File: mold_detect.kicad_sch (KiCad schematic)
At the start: 22 parts, among them J1 ISP, SW1 watchdog_sw, U1 SHT30-DIS, U2 TPL5010, U3 ATmega328P-P

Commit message: added ces reference; moved sensor to bottom
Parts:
- R1, R2, R3, R4, R5, R6: footprint Resistor_SMD:R_0201_0603Metric -> Resistor_SMD:R_0603_1608Metric
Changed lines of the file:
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@@
       (effects (font (size 1.27 1.27)) (justify left))
     )
-    (property "Footprint" "Resistor_SMD:R_0201_0603Metric" (at 254.762 73.66 90)
+    (property "Footprint" "Resistor_SMD:R_0603_1608Metric" (at 254.762 73.66 90)
       (effects (font (size 1.27 1.27)) hide)
     )
@@
       (effects (font (size 1.27 1.27)) (justify left))
     )
-    (property "Footprint" "Resistor_SMD:R_0201_0603Metric" (at 60.452 170.18 90)
+    (property "Footprint" "Resistor_SMD:R_0603_1608Metric" (at 60.452 170.18 90)
       (effects (font (size 1.27 1.27)) hide)
     )
@@
       (effects (font (size 1.27 1.27)) (justify left))
     )
-    (property "Footprint" "Resistor_SMD:R_0201_0603Metric" (at 93.472 59.69 90)
+    (property "Footprint" "Resistor_SMD:R_0603_1608Metric" (at 93.472 59.69 90)
       (effects (font (size 1.27 1.27)) hide)
     )
@@
       (effects (font (size 1.27 1.27)) (justify left))
     )
-    (property "Footprint" "Resistor_SMD:R_0201_0603Metric" (at 238.252 73.66 90)
+    (property "Footprint" "Resistor_SMD:R_0603_1608Metric" (at 238.252 73.66 90)
       (effects (font (size 1.27 1.27)) hide)
     )
@@
       (effects (font (size 1.27 1.27)) (justify left))
     )
-    (property "Footprint" "Resistor_SMD:R_0201_0603Metric" (at 245.872 73.66 90)
+    (property "Footprint" "Resistor_SMD:R_0603_1608Metric" (at 245.872 73.66 90)
       (effects (font (size 1.27 1.27)) hide)
     )
@@
       (effects (font (size 1.27 1.27)) (justify left))
     )
-    (property "Footprint" "Resistor_SMD:R_0201_0603Metric" (at 80.772 170.18 90)
-      (effects (font (size 1.27 1.27)) hide)
-    )
+    (property "Footprint" "Resistor_SMD:R_0603_1608Metric" (at 80.772 170.18 90)
+      (effects (font (size 1.27 1.27)) hide)
+    )

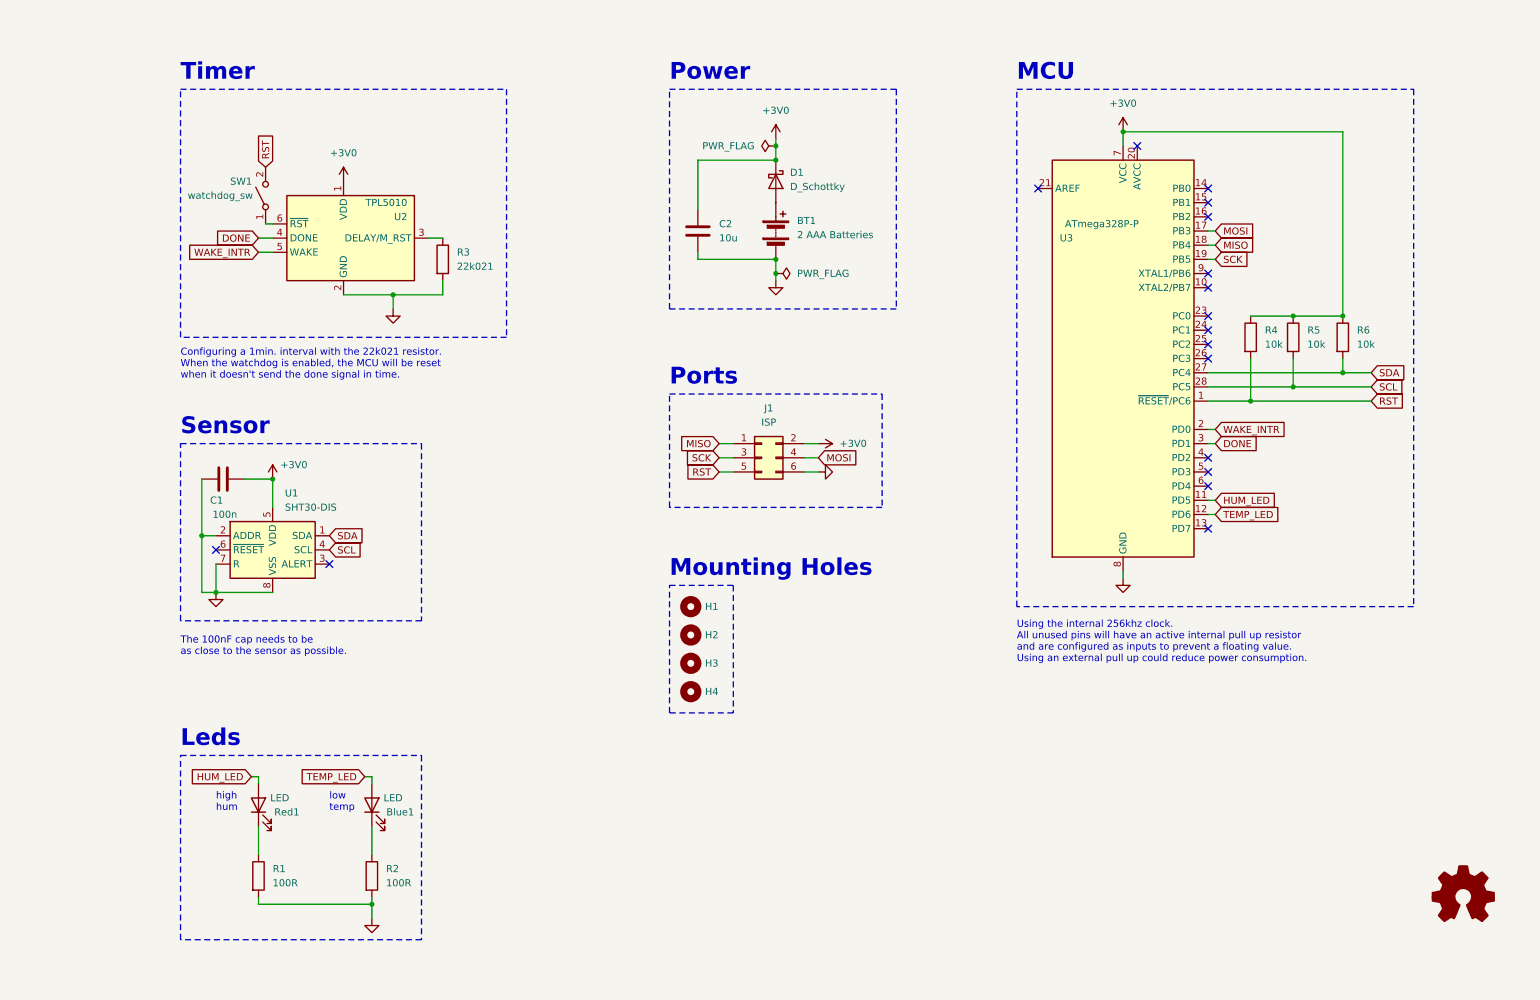
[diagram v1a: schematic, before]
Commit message: removed isp; added uart; added flash
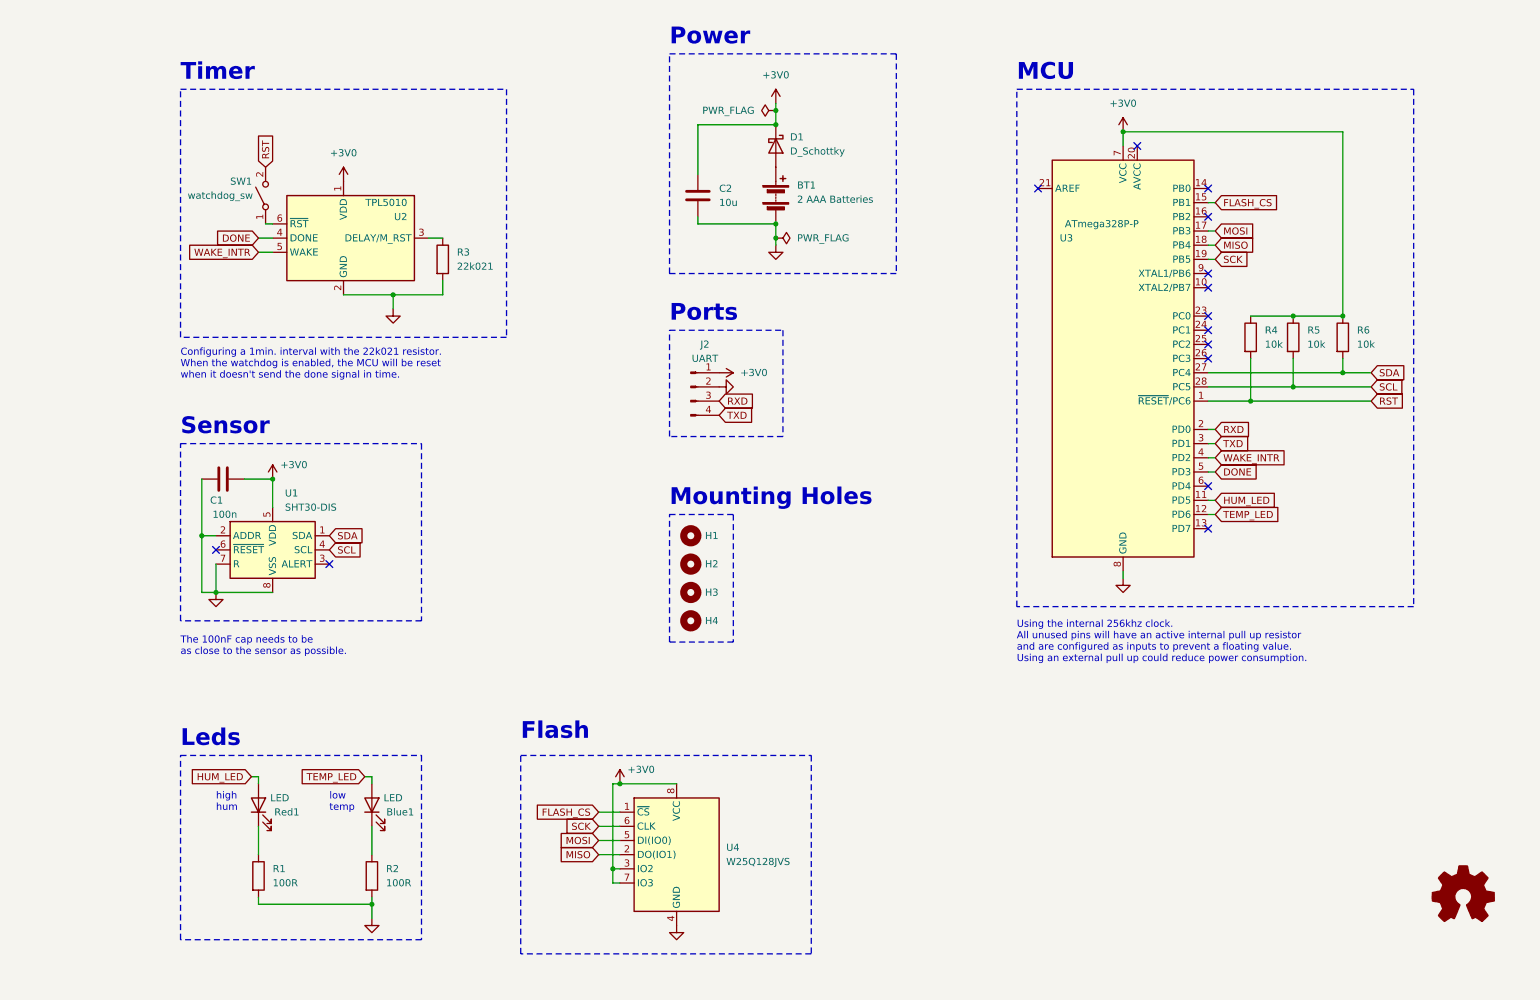
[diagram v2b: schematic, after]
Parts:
- removed J1: ISP, Connector_IDC:IDC-Header_2x03_P2.54mm_Vertical, symbol Connector_Generic:Conn_02x03_Odd_Even
- added J2: UART, Connector_PinHeader_2.54mm:PinHeader_1x04_P2.54mm_Vertical, symbol Connector:Conn_01x04_Pin
- added U4: W25Q128JVS, Package_SO:SOIC-8_5.23x5.23mm_P1.27mm, symbol Memory_Flash:W25Q128JVS
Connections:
- net +3V0: now also J2.1 (Pin_1), U4.3 (IO2), U4.7 (IO3), U4.8 (VCC)
- net DONE: now also U3.5 (PD3); no longer U3.3 (PD1)
- net GND: now also J2.2 (Pin_2), U4.4 (GND)
- net MISO: now also U4.2 (DO(IO1))
- net MOSI: now also U4.5 (DI(IO0))
- net SCK: now also U4.6 (CLK)
- net WAKE_INTR: now also U3.4 (PD2); no longer U3.2 (PD0)
- net FLASH_CS: now reaches U3.15 (PB1)
- net FLASH_CS: now also U4.1 (~{CS})
- new net RXD: J2.3 (Pin_3), U3.2 (PD0)
- new net TXD: J2.4 (Pin_4), U3.3 (PD1)
- no-connect marks 17 -> 14
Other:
- note added: "Flash"
- moved on the sheet: BT1, C2, D1, H1, H2, H3, H4

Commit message: added usb c port
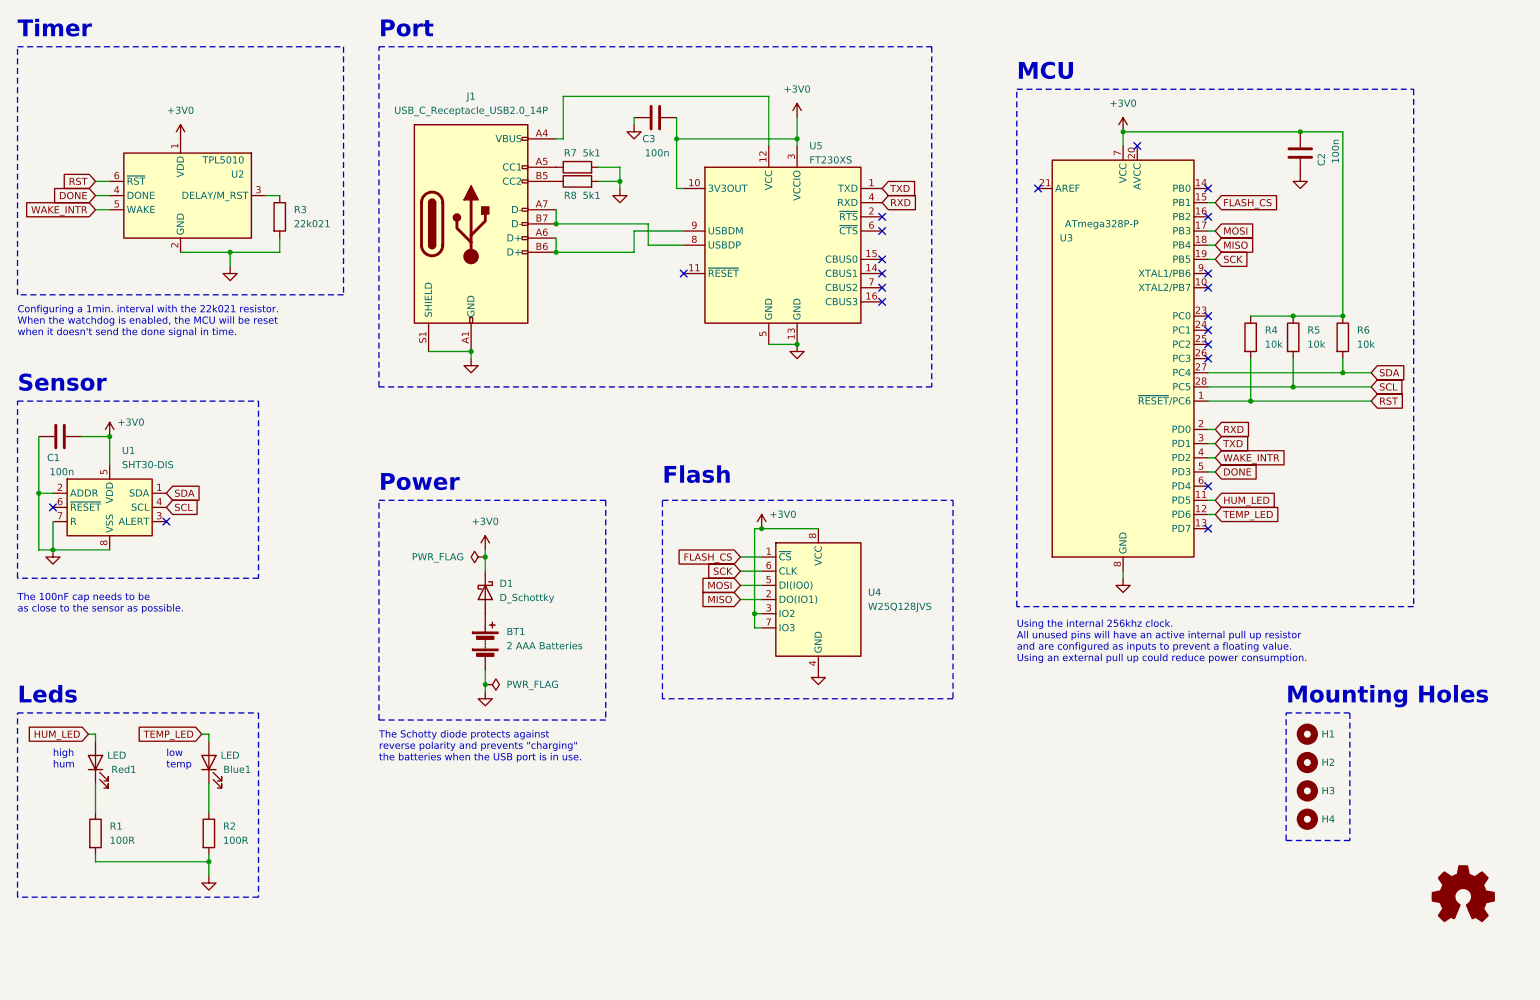
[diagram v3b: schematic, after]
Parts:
- removed J2: UART, Connector_PinHeader_2.54mm:PinHeader_1x04_P2.54mm_Vertical, symbol Connector:Conn_01x04_Pin
- removed SW1: watchdog_sw, Button_Switch_SMD:SW_DIP_SPSTx01_Slide_6.7x4.1mm_W6.73mm_P2.54mm_LowProfile_JPin, symbol Switch:SW_SPST
- added C3: 100n, Capacitor_SMD:C_0603_1608Metric_Pad1.08x0.95mm_HandSolder, symbol Device:C
- added J1: USB_C_Receptacle_USB2.0_14P, Connector_USB:USB_C_Receptacle_GCT_USB4105-xx-A_16P_TopMnt_Horizontal, symbol Connector:USB_C_Receptacle_USB2.0_14P
- added R7, R8: 5k1, Resistor_SMD:R_0603_1608Metric_Pad0.98x0.95mm_HandSolder, symbol Device:R
- added U5: FT230XS, Package_SO:SSOP-16_3.9x4.9mm_P0.635mm, symbol Interface_USB:FT230XS
- C1: footprint Capacitor_SMD:C_0805_2012Metric -> Capacitor_SMD:C_0603_1608Metric_Pad1.08x0.95mm_HandSolder
- C2: value 10u -> 100n; footprint Capacitor_SMD:C_0805_2012Metric -> Capacitor_SMD:C_0603_1608Metric_Pad1.08x0.95mm_HandSolder
- D1: footprint Diode_SMD:D_SOD-323F -> Diode_SMD:D_SOD-323_HandSoldering
- R1, R2, R3, R4, R5, R6: footprint Resistor_SMD:R_0603_1608Metric -> Resistor_SMD:R_0603_1608Metric_Pad0.98x0.95mm_HandSolder
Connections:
- net +3V0: now also C2.2, C3.2, U5.10 (3V3OUT), U5.3 (VCCIO); no longer C2.1
- net GND: now also C2.1, C3.1, J1.A1 (GND), J1.A12 (GND), J1.B1 (GND), J1.B12 (GND), J1.S1 (SHIELD), R7.2, R8.2, U5.13 (GND), U5.5 (GND); no longer C2.2
- net RST: now also U2.6 (~{RST})
- net RXD: now also U5.4 (RXD)
- net TXD: now also U5.1 (TXD)
- new net: J1.B5 (CC2), R8.1
- new net: J1.A4 (VBUS), J1.A9 (VBUS), J1.B4 (VBUS), J1.B9 (VBUS), U5.12 (VCC)
- new net: J1.A5 (CC1), R7.1
- new net: J1.A6 (D+), J1.B6 (D+), U5.9 (USBDM)
- new net: J1.A7 (D-), J1.B7 (D-), U5.8 (USBDP)
- no-connect marks 14 -> 21
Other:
- note added: "Port"
- note added: "The Schotty diode protects against reverse polarity and prevents "charging" the batteries when the USB port is in use."
- note removed: "Ports"
- moved on the sheet: BT1, Blue1, C1, D1, H1, H2, H3, H4, R1, R2, R3, Red1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

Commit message: changed usb-c port to match "USB Bus Powered Configuration" from p. 18
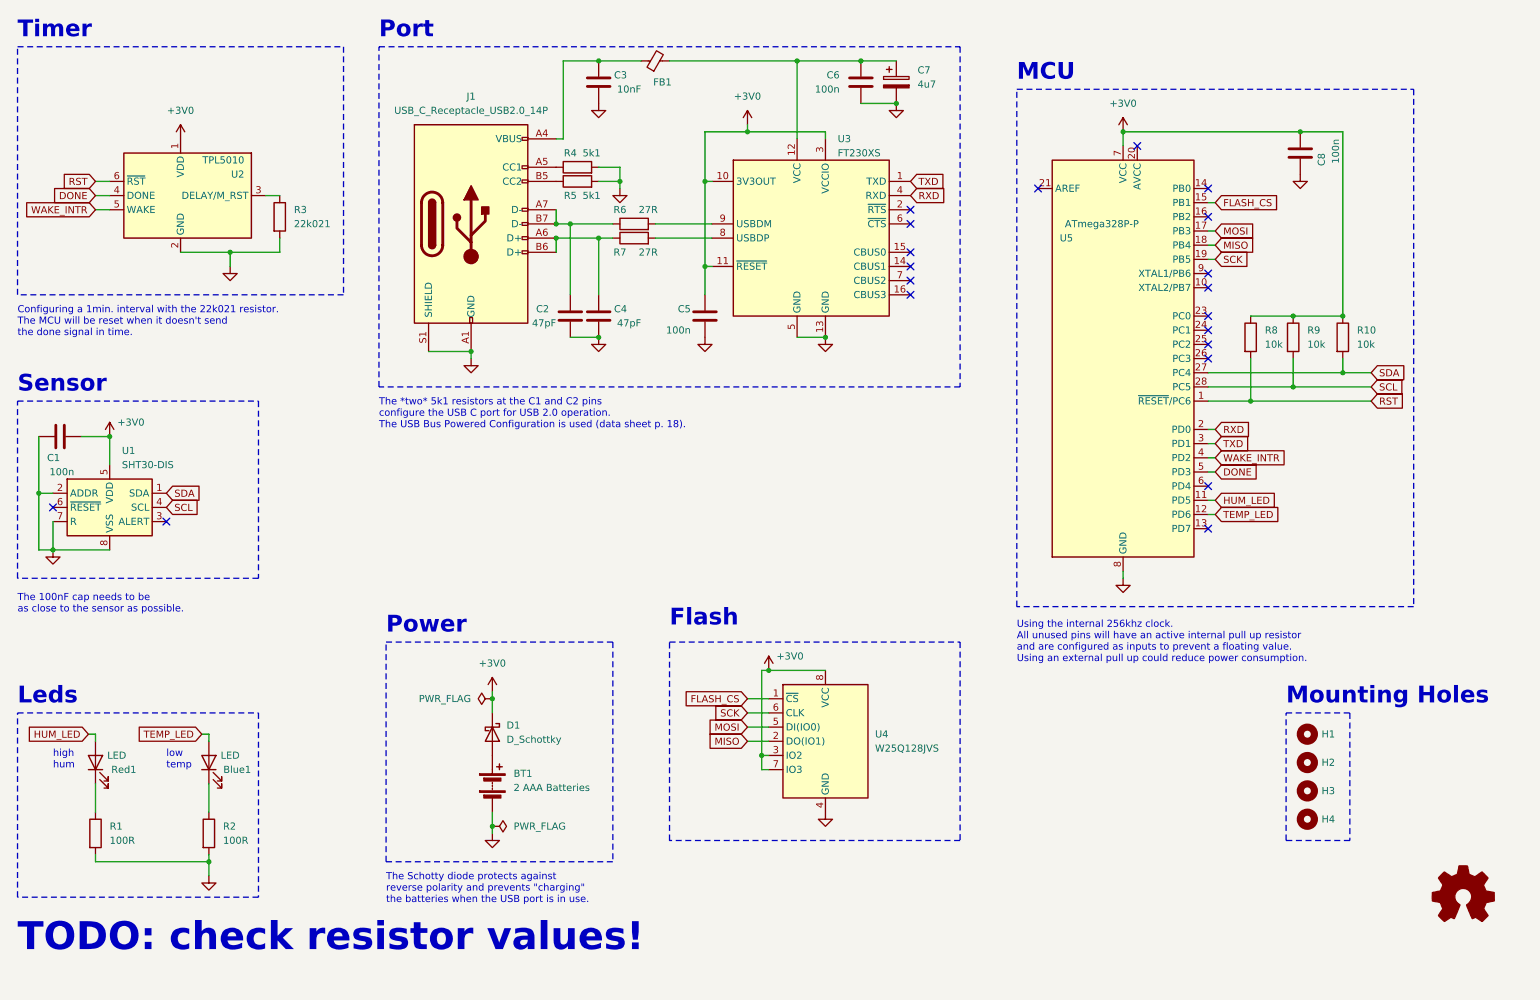
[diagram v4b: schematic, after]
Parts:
- added C2, C4: 47pF, Capacitor_SMD:C_0603_1608Metric_Pad1.08x0.95mm_HandSolder, symbol Device:C
- added C5, C6: 100n, Capacitor_SMD:C_0603_1608Metric_Pad1.08x0.95mm_HandSolder, symbol Device:C
- added C7: 4u7, symbol Device:C_Polarized
- added FB1: ~, symbol Device:FerriteBead_Small
- added R6, R7: 27R, Resistor_SMD:R_0603_1608Metric_Pad0.98x0.95mm_HandSolder, symbol Device:R
- C3: value 100n -> 10nF
- renumbered C2 to C8, R6 to R10, R7 to R4, R8 to R5, R4 to R8, R5 to R9, U5 to U3, U3 to U5
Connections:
- net +3V0: now also U3.11 (~{RESET}), C5.2; no longer C3.2
- net GND: now also C2.1, C4.1, C5.1, C6.1, C7.2
- net at J1.A4 (VBUS), J1.A9 (VBUS), J1.B4 (VBUS)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: now also C3.2, FB1.1; no longer U3.12 (VCC)
- net at J1.A6 (D+), J1.B6 (D+): now also C4.2, R7.1; no longer U3.9 (USBDM)
- net at J1.A7 (D-), J1.B7 (D-): now also C2.2, R6.1; no longer U3.8 (USBDP)
- new net: R7.2, U3.8 (USBDP)
- new net: C6.2, C7.1, FB1.2, U3.12 (VCC)
- new net: R6.2, U3.9 (USBDM)
- no-connect marks 21 -> 20
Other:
- note added: "Configuring a 1min. interval with the 22k021 resistor. The MCU will be reset when it doesn't send the done signal in time."
- note added: "TODO: check resistor values!"
- note added: "The *two* 5k1 resistors at the C1 and C2 pins configure the USB C port for USB 2.0 operation. The USB Bus Powered Configuration is used (data sheet p. 18)."
- note removed: "Configuring a 1min. interval with the 22k021 resistor. When the watchdog is enabled, the MCU will be reset when it doesn't send the done signal in time."
- moved on the sheet: BT1, D1, U3, U4
